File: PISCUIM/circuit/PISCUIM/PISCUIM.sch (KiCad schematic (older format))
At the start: 76 parts, among them CON1 BARREL_JACK, CON10 BARREL_JACK, CON11 BARREL_JACK, CON12 BARREL_JACK, CON13 BARREL_JACK, CON14 BARREL_JACK, CON15 BARREL_JACK, CON16 BARREL_JACK, CON17 BARREL_JACK, CON18 BARREL_JACK, CON19 BARREL_JACK, CON2 BARREL_JACK, CON20 BARREL_JACK, CON21 BARREL_JACK, CON22 BARREL_JACK, CON23 BARREL_JACK, CON24 BARREL_JACK, CON3 BARREL_JACK, CON4 BARREL_JACK, CON5 BARREL_JACK, CON6 BARREL_JACK, CON7 BARREL_JACK, CON8 BARREL_JACK, CON9 BARREL_JACK, IC1 PIC16F1938, P1 CONN_01X06, P2 CONN_01X06, P3 CONN_01X08, P4 CONN_01X08, P5 CONN_01X06, Q1 EKI04047, Q10 EKI04047, Q11 EKI04047, Q12 EKI04047, Q13 EKI04047, Q14 EKI04047, Q15 EKI04047, Q16 EKI04047, Q17 EKI04047, Q18 EKI04047, Q19 EKI04047, Q2 EKI04047, Q20 EKI04047, Q3 EKI04047, Q4 EKI04047, Q5 EKI04047, Q6 EKI04047, Q7 EKI04047, Q8 EKI04047, Q9 EKI04047

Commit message: PISCUIM circuit power line modified
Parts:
- removed CON3, CON5, CON7, CON9: BARREL_JACK, Connect:BARREL_JACK, symbol BARREL_JACK
- added P8: GINGA_voltage_selector, symbol CONN_01X03
- gave numbers to parts that had none: 2
- renumbered CON18 to CON10, CON19 to CON11, CON20 to CON12, CON21 to CON13, CON22 to CON14, CON23 to CON15, CON24 to CON16, CON4 to CON17, CON6 to CON18, CON8 to CON19, CON10 to CON20, CON11 to CON3, CON12 to CON4, CON13 to CON5, CON14 to CON6, CON15 to CON7, CON16 to CON8, CON17 to CON9, P5 to P1, P1 to P2, P2 to P3, P3 to P5, P4 to P6, Q14 to Q10, Q15 to Q11, Q16 to Q12, Q17 to Q13, Q18 to Q14, Q19 to Q15, Q20 to Q16, Q5 to Q17, Q6 to Q18, Q7 to Q19, Q8 to Q20, Q9 to Q5, Q10 to Q6, Q11 to Q7, Q12 to Q8, Q13 to Q9, R14 to R10, R15 to R11, R16 to R12, R17 to R13, R18 to R14, R19 to R15, R20 to R16, R21 to R17, R6 to R18, R7 to R19, R8 to R20, R9 to R21, R10 to R6, R11 to R7, R12 to R8, R13 to R9, RR3 to RR2, RR2 to RR3
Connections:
- net +12V: now also P4.5 (P5), P4.6 (P6), P4.7 (P7), P4.8 (P8), P7.5 (P5), P7.6 (P6), P7.7 (P7), P7.8 (P8); no longer CON1.1, CON10.1, CON11.1, CON12.1, CON13.1, CON14.1, CON15.1, CON16.1, CON2.1, CON3.1, CON4.1, CON5.1, CON6.1, CON7.1, CON8.1, CON9.1, IC1.20 (PIN20), P1.2 (P2), P2.4 (P4), P3.3 (P3), P5.8 (P8), R17.1
- net 12V_KOUTOU11: now reaches CON17.1
- net 12V_KOUTOU11: now also P4.1 (P1), P4.2 (P2)
- net 12V_KOUTOU21: now reaches CON18.1
- net 12V_KOUTOU21: now also P4.3 (P3), P4.4 (P4)
- net 5V_ITTOU1: now reaches CON19.1
- net 5V_ITTOU1: now also P7.1 (P1), P7.2 (P2)
- net VCC_GINGA: now reaches CON20.1
- net VCC_GINGA: now also P8.2 (P2)
- net 12V_SEIZAE1: now reaches P4.10 (P10)
- net 12V_SEIZAE1: now also CON1.1, CON10.1, CON11.1, CON12.1, CON13.1, CON14.1, CON15.1, CON16.1, CON2.1, CON3.1, CON4.1, CON5.1, CON6.1, CON7.1, CON8.1, CON9.1, P4.9 (P9)
- net 3.3V_LOGIC: now reaches P7.10 (P10)
- net 3.3V_LOGIC: now also P3.3 (P3), P5.8 (P8)
- net 5V_GINGA: now reaches P7.3 (P3)
- net 5V_GINGA: now also P8.1 (P1)
- net 12V_GINGA: now reaches P7.4 (P4)
- net 12V_GINGA: now also P8.3 (P3)
- net 5V_LOGIC: now reaches P7.9 (P9)
- net 5V_LOGIC: now also IC1.20 (PIN20), P1.2 (P2), P2.4 (P4), R17.1
- no-connect marks 48 -> 44
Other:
- moved on the sheet: P4

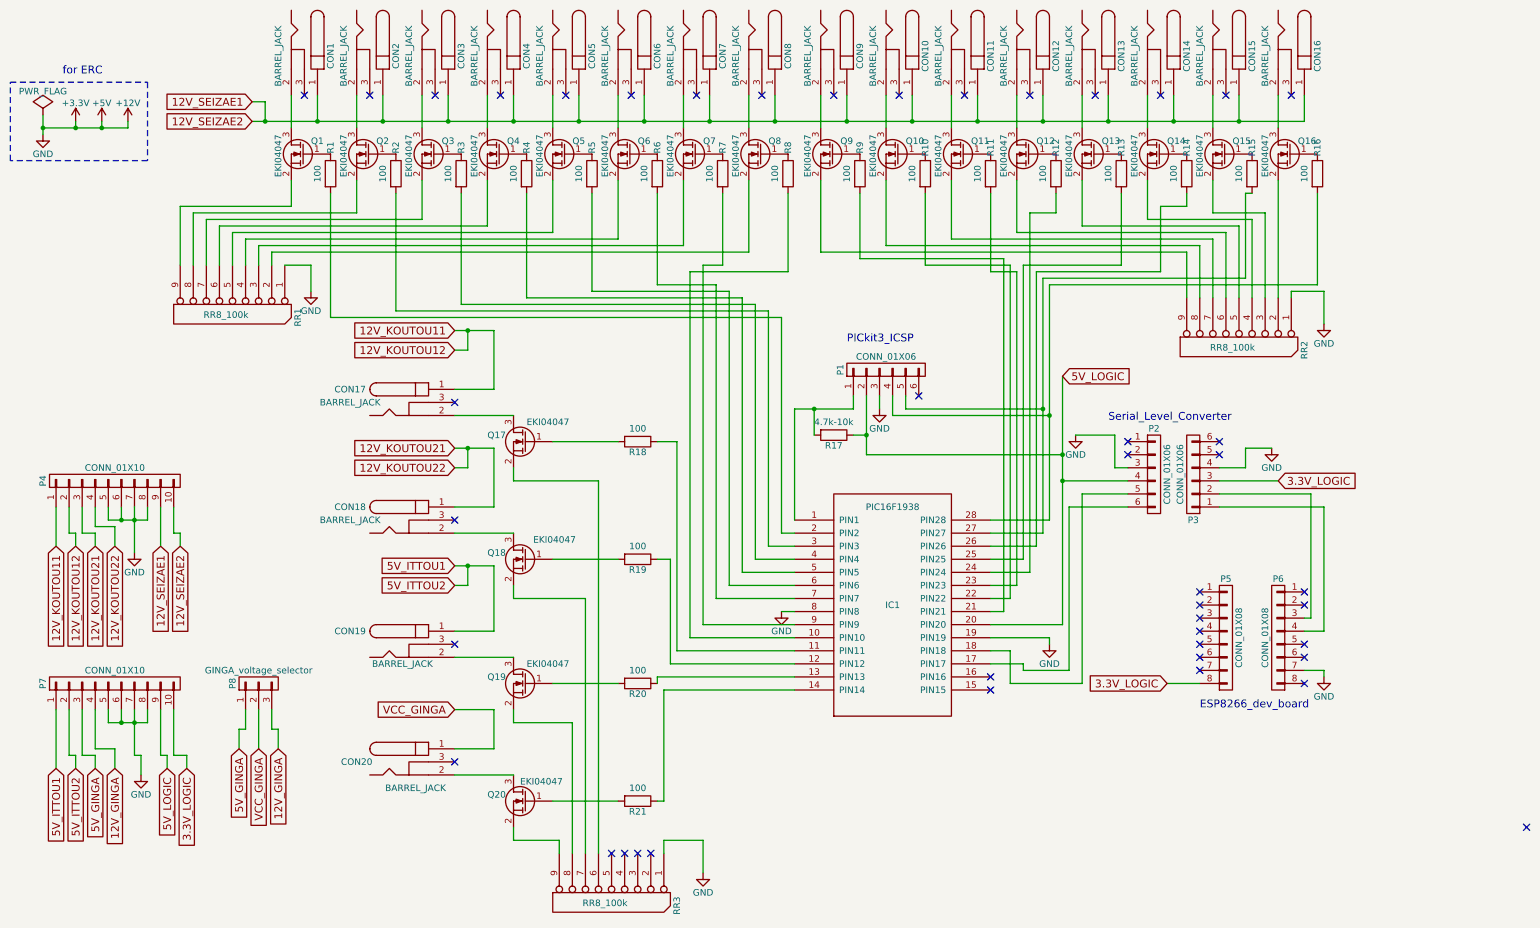
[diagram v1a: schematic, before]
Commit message: fixed fatal mistake in diagram
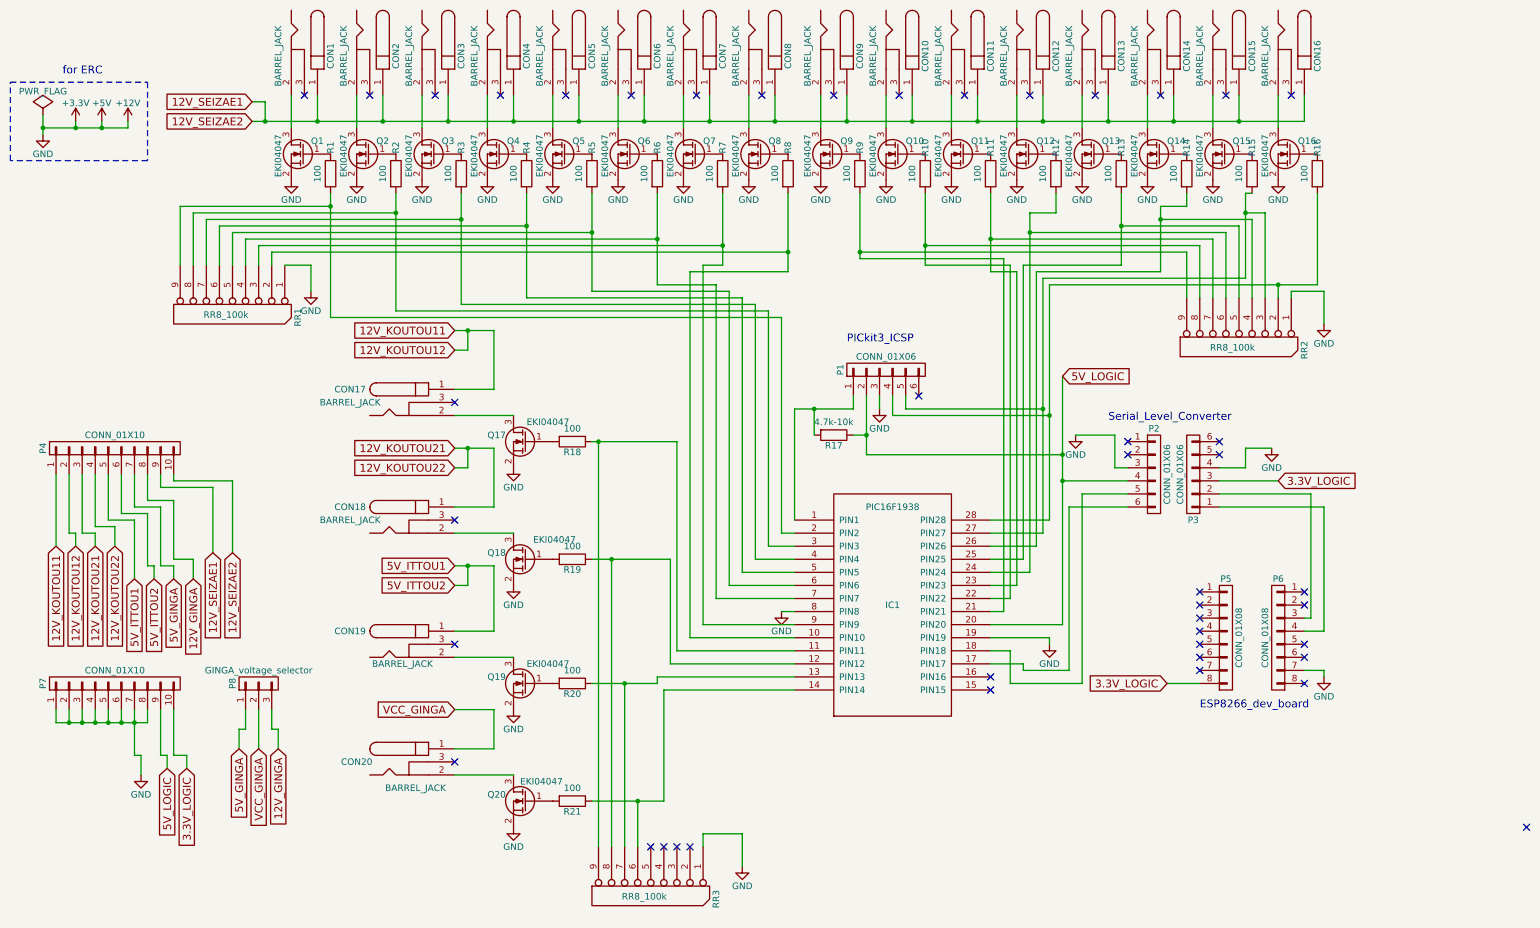
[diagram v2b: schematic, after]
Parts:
- P1, P2, P3: footprint (none) -> Pin_Headers:Pin_Header_Straight_1x06
- P4, P7: footprint (none) -> Pin_Headers:Pin_Header_Straight_1x10
- P8: footprint (none) -> Pin_Headers:Pin_Header_Straight_1x03
- R17: footprint (none) -> Resistors_ThroughHole:Resistor_Horizontal_RM7mm
- RR1, RR2, RR3: footprint (none) -> Resistors_ThroughHole:Resistor_Array_SIP8
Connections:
- net +12V: now also P7.1 (P1), P7.2 (P2), P7.3 (P3), P7.4 (P4), Q1.2 (S), Q10.2 (S), Q11.2 (S), Q12.2 (S), Q13.2 (S), Q14.2 (S), Q15.2 (S), Q16.2 (S), Q17.2 (S), Q18.2 (S), Q19.2 (S), Q2.2 (S), Q20.2 (S), Q3.2 (S), Q4.2 (S), Q5.2 (S), Q6.2 (S), Q7.2 (S), Q8.2 (S), Q9.2 (S); no longer P4.5 (P5), P4.6 (P6), P4.7 (P7), P4.8 (P8)
- net 12V_GINGA: now also P4.8 (P8); no longer P7.4 (P4)
- net 5V_GINGA: now also P4.7 (P7); no longer P7.3 (P3)
- net 5V_ITTOU1: now also P4.5 (P5), P4.6 (P6); no longer P7.1 (P1), P7.2 (P2)
- net at IC1.10 (PIN10), R8.2: now also RR1.2
- net at IC1.11 (PIN11), R18.1: now also RR3.9
- net at IC1.12 (PIN12), R19.1: now also RR3.8
- net at IC1.13 (PIN13), R20.1: now also RR3.7
- net at IC1.14 (PIN14), R21.1: now also RR3.6
- net at IC1.2 (PIN2), R1.2: now also RR1.9
- net at IC1.21 (PIN21), R9.2: now also RR2.9
- net at IC1.22 (PIN22), R10.2: now also RR2.8
- net at IC1.23 (PIN23), R11.2: now also RR2.7
- net at IC1.24 (PIN24), R12.2: now also RR2.6
- net at IC1.25 (PIN25), R13.2: now also RR2.5
- net at IC1.26 (PIN26), R14.2: now also RR2.4
- net at IC1.27 (PIN27), P1.5 (P5), R15.2: now also RR2.3
- net at IC1.28 (PIN28), P1.4 (P4), R16.2: now also RR2.2
- net at IC1.3 (PIN3), R2.2: now also RR1.8
- net at IC1.4 (PIN4), R3.2: now also RR1.7
- net at IC1.5 (PIN5), R4.2: now also RR1.6
- net at IC1.6 (PIN6), R5.2: now also RR1.5
- net at IC1.7 (PIN7), R6.2: now also RR1.4
- net at IC1.9 (PIN9), R7.2: now also RR1.3
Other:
- moved on the sheet: P4, R18, R19, R20, R21, RR3

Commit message: modified circuit diagram and made little changes in code(unfinished)
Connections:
- net +12V: now also P4.7 (P7), P4.8 (P8), P7.10 (P10), P7.9 (P9); no longer P7.1 (P1), P7.2 (P2), P7.3 (P3), P7.4 (P4)
- net 12V_GINGA: now also P7.2 (P2); no longer P4.8 (P8)
- net 3.3V_LOGIC: now also P7.4 (P4); no longer P7.10 (P10)
- net 5V_GINGA: now also P7.1 (P1); no longer P4.7 (P7)
- net 5V_LOGIC: now also P7.3 (P3); no longer P7.9 (P9)
- net at IC1.11 (PIN11), R18.1: now also RR3.6; no longer RR3.9
- net at IC1.12 (PIN12), R19.1: now also RR3.5; no longer RR3.8
- net at IC1.13 (PIN13), R20.1: now also RR3.4; no longer RR3.7
- net at IC1.14 (PIN14), R21.1: now also RR3.3; no longer RR3.6
- net at P6.1 (P1): now also P3.2 (P2)
- net at P6.2 (P2): now also P3.1 (P1)
- net at P6.3 (P3): no longer P3.2 (P2)
- net at P6.4 (P4): no longer P3.1 (P1)

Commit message: minor change in power line
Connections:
- net +12V: no longer P7.5 (P5)
- net 12V_SEIZAE1: now also P7.5 (P5)
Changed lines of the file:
@@
 	2650 1350 2750 1350
 Wire Wire Line
-	2750 1350 2750 1500
+	2750 1350 2750 1650
 Connection ~ 2750 1500
 Wire Wire Line
@@
 	2500 4250 2500 4800
 Connection ~ 1750 6100
-Wire Wire Line
-	1550 6100 2050 6100
 $Comp
 L GND #PWR036
@@
 	1150 6150 1150 6000
 Wire Wire Line
-	1550 6000 1550 6100
-Wire Wire Line
 	1650 6000 1650 6100
-Connection ~ 1650 6100
 NoConn ~ 10700 5300
 NoConn ~ 10700 5400
@@
 NoConn ~ 5500 7050
 NoConn ~ 6000 7050
+Wire Wire Line
+	1650 6100 2050 6100
+Text GLabel 1700 6400 3    60   Input ~ 0
+12V_SEIZAE3
+Wire Wire Line
+	1550 6000 1550 6150
+Wire Wire Line
+	1550 6150 1700 6150
+Wire Wire Line
+	1700 6150 1700 6400
+Text GLabel 2650 1650 0    60   Input ~ 0
+12V_SEIZAE3
+Wire Wire Line
+	2750 1650 2650 1650
 $EndSCHEMATC
